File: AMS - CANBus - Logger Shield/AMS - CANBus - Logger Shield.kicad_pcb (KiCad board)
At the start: 2 copper layers, 68.6 x 53.3 mm, 33 parts, among them IC1 DS3231SN#, IC4 CD74HC4050ME4, J1 Power, J2 Digital/PWM, J3 Analog, J4 Digital/PWM, J5 Power_And_CAN, J6 GTFH08131YHR, J7 Conn_01x02, Q1 IRF9Z34NPBF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

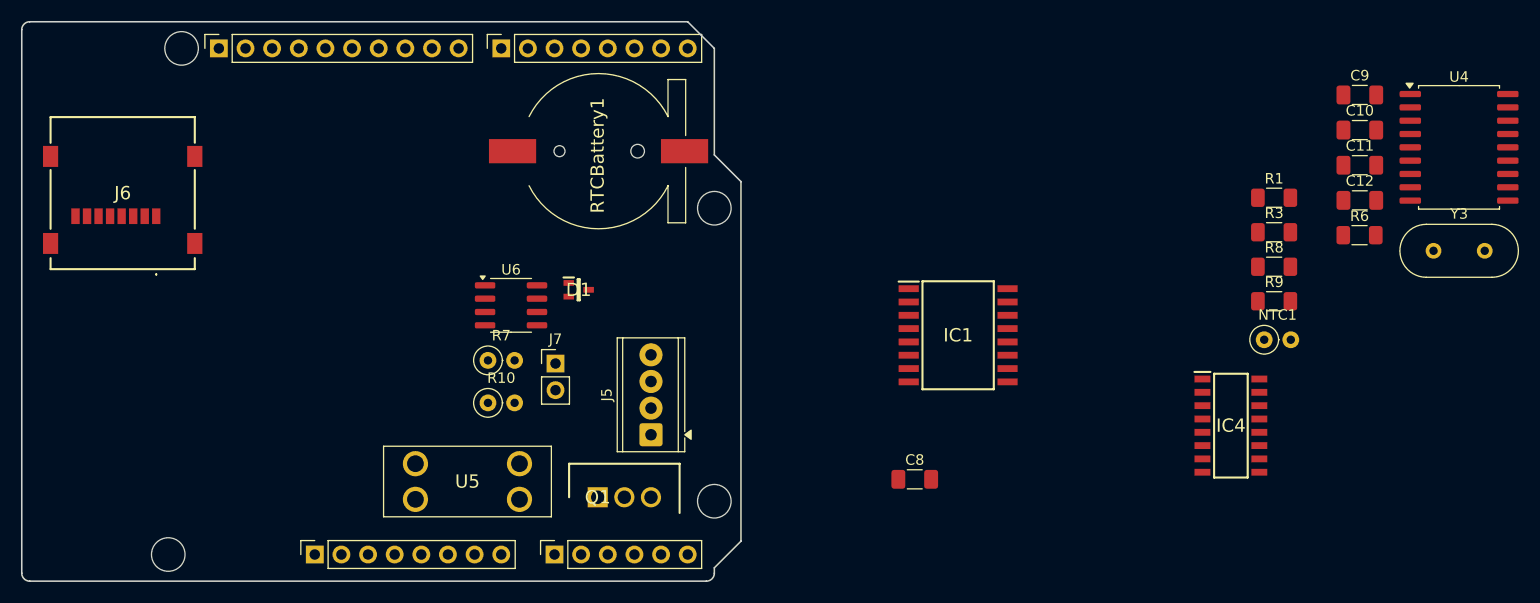
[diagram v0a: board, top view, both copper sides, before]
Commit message: logger shield routed
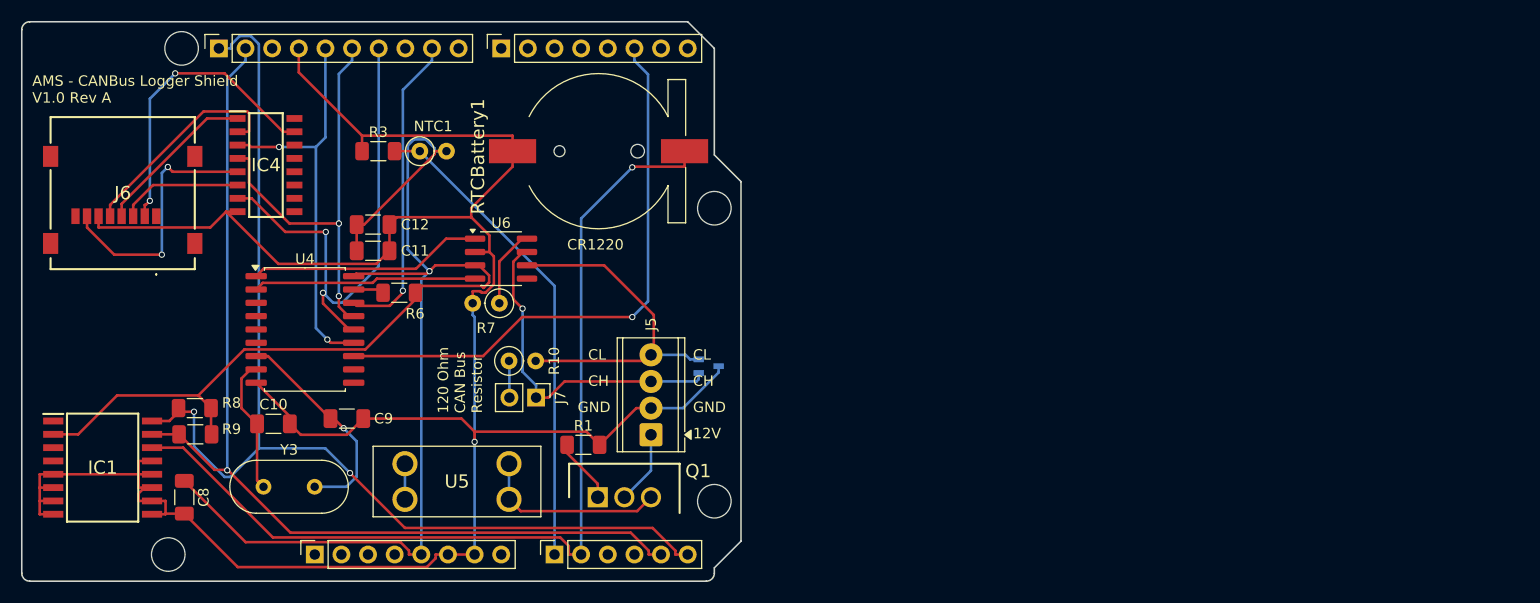
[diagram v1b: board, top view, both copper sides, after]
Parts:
- D1: moved to B.Cu
- moved Y3 113.8 mm to (123.0, 91.0)
- moved U4 111.4 mm to (127.0, 76.0)
- moved C10 107.3 mm to (124.0, 85.0)
- moved R8 103.8 mm to (116.5, 83.5), turned to 180 degrees
- moved R9 103.6 mm to (116.5, 86.0), turned to 180 degrees
- moved C9 101.4 mm to (131.0, 84.5)
- moved IC4 95.3 mm to (123.3, 60.3)
- moved C11 94.4 mm to (133.5, 68.5)
- moved C12 94.1 mm to (133.5, 66.0)
- moved R6 91.7 mm to (136.0, 72.5)
- moved R3 85.8 mm to (134.0, 59.0)
- moved IC1 82.5 mm to (107.7, 89.2)
- moved NTC1 82.5 mm to (138.0, 59.0)
- moved R1 70.0 mm to (153.6, 87.0)
- moved C8 69.7 mm to (115.5, 92.0), turned to -90 degrees
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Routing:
- net GND: track 0.00 -> 231.1 mm, vias 0 -> 1
- net +5V: track 0.00 -> 151.3 mm, vias 0 -> 1
- net SCL: track 0.00 -> 105.2 mm, vias 0 -> 2
- net SDA: track 0.00 -> 94.5 mm, vias 0 -> 1
- net /A1: track 0.00 -> 91.0 mm, vias 0 -> 1
- net /2: track 0.00 -> 54.9 mm, vias 0 -> 1
- net MOSI5V: track 0.00 -> 48.7 mm, vias 0 -> 2
- net /A0: track 0.00 -> 46.2 mm
- net MISO5V: track 0.00 -> 40.5 mm, vias 0 -> 2
- net CLK5V: track 0.00 -> 38.8 mm, vias 0 -> 2
- net CANBUS_L: track 0.00 -> 33.9 mm
- net CANBUS_H: track 0.00 -> 32.4 mm, vias 0 -> 1
- net CANBusCS: track 0.00 -> 29.8 mm, vias 0 -> 1
- net SDCS3.3V: track 0.00 -> 28.6 mm, vias 0 -> 2
- net MISO3.3V: track 0.00 -> 24.7 mm, vias 0 -> 2
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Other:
- board text added: "120 Ohm CAN Bus Resistor"
- board text added: "12V"
- board text added: "AMS - CANBus Logger Shield V1.0 Rev A"
- board text added: "CH"
- board text added: "CL"
- board text added: "CR1220"
- board text added: "GND"

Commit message: Logger Shield fixing the following Fuck ups for 1.0 Rev A * didn't connect the 3.3v lines * didn't connect the 5.5v SD Card Chip Select to the level shifter * didn't connect the VDC to the Vin pin
Did some route optimization with my widdle brain.
Bumped to Rev B since i didn't fix any that was not a complete fuck up or add anything new
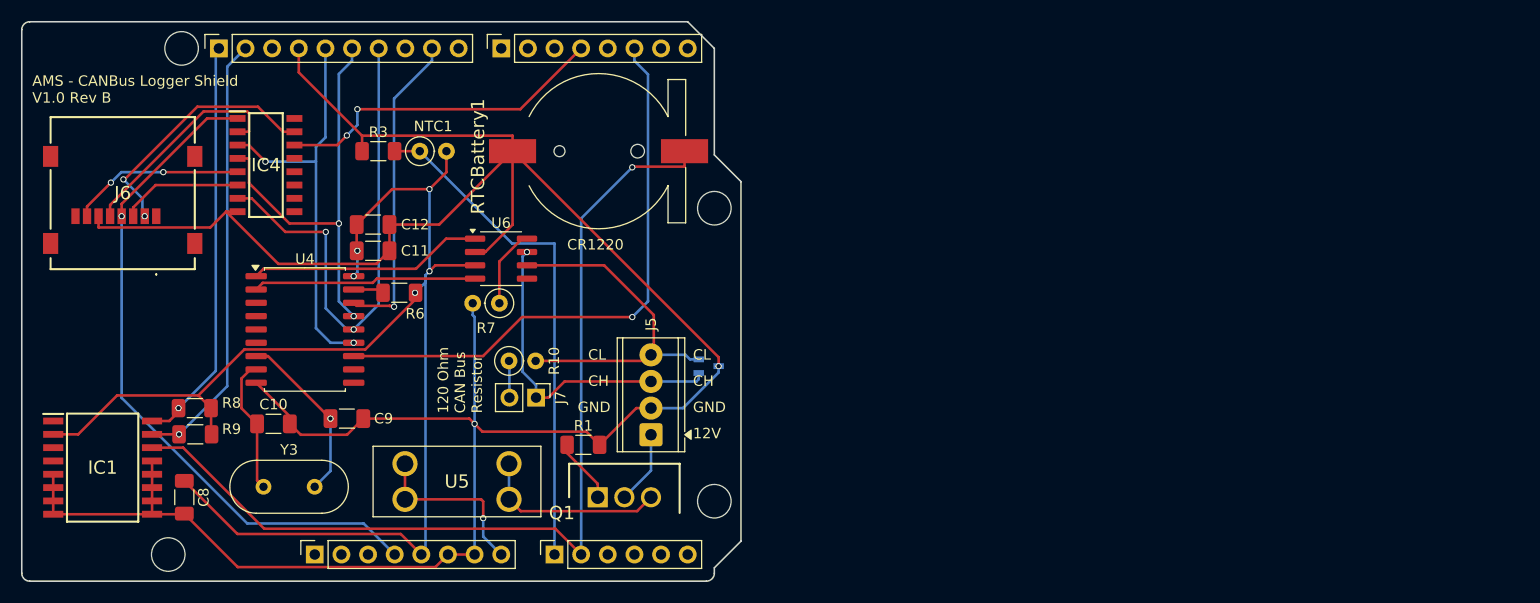
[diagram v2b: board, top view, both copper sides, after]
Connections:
- IC4 pad 1: +3.3V -> +3V3
- J3 pad 5: SDA -> unconnected-(J3-Pin_5-Pad5)
- J3 pad 6: SCL -> unconnected-(J3-Pin_6-Pad6)
- J4 pad 4: /4 -> SDCS5V
- J6 pad 4: +3.3V -> +3V3
- U5 pad 3: +VDC -> VCC
- U5 pad 4: +VDC -> VCC
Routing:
- net SCL: track 105.2 -> 39.1 mm, vias 2 -> 1
- net +3V3: track 0.00 -> 65.1 mm, vias 0 -> 1
- net SDA: track 94.5 -> 42.0 mm
- net SDCS5V: track 0.00 -> 32.0 mm, vias 0 -> 2
- net +5V: track 151.3 -> 129.8 mm, vias 1 -> 5
- net VCC: track 0.00 -> 16.7 mm, vias 0 -> 1
- net +3.3V: track 15.6 -> 0.00 mm
- net GND: track 231.1 -> 246.1 mm, vias 1 -> 2
- net MISO3.3V: track 24.7 -> 16.6 mm
- net SDCS3.3V: track 28.6 -> 24.5 mm
- net Net-(U4-OSC2): track 20.7 -> 16.7 mm
- net +VDC: track 3.40 -> 0.00 mm
- net /A0: track 46.2 -> 48.6 mm
- net CANBUS_H: track 32.4 -> 31.4 mm
- net CLK5V: track 38.8 -> 39.4 mm
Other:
- board text added: "AMS - CANBus Logger Shield V1.0 Rev B"
- board text removed: "AMS - CANBus Logger Shield V1.0 Rev A"
